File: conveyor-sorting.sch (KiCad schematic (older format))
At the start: 17 parts

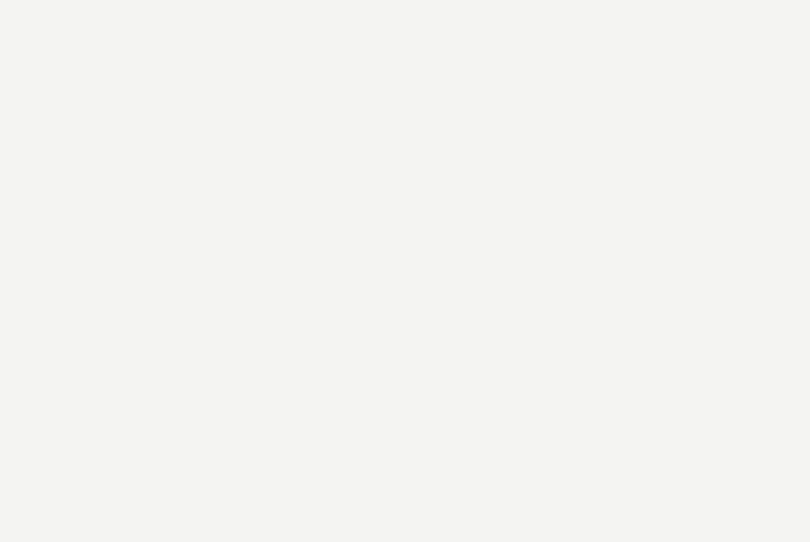
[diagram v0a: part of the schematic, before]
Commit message: Added l293d lib
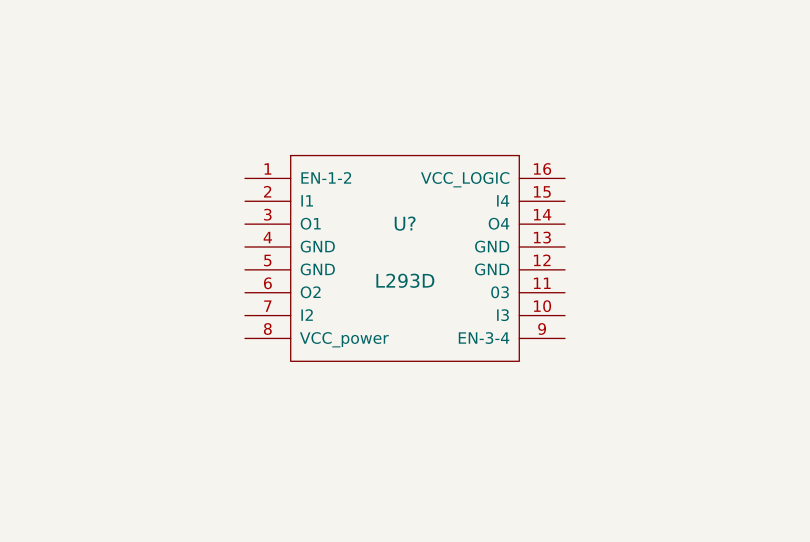
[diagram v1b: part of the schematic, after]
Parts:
- added U?: L293D, symbol L293D
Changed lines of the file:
@@
 LIBS:contrib
 LIBS:valves
+LIBS:l293d
+LIBS:conveyor-sorting-cache
 EELAYER 25 0
 EELAYER END
@@
 Text Label 6700 4400 2    60   ~ 0
 M3_Signal
+$Comp
+L L293D U?
+U 1 1 58CEFBD8
+P 7650 2200
+F 0 "U?" H 7650 2350 60  0000 C CNN
+F 1 "L293D" H 7650 2100 60  0000 C CNN
+F 2 "" H 7650 2000 60  0001 C CNN
+F 3 "" H 7650 2000 60  0001 C CNN
+	1    7650 2200
+	1    0    0    -1
+$EndComp
 $EndSCHEMATC

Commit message: rev 1 done
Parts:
- removed U?: L293D, symbol L293D
- added P1, P2: CONN_01X02, Terminal_Blocks:TerminalBlock_Pheonix_MKDS1.5-2pol, symbol CONN_01X02
- added P15: CONN_01X07, Connectors_Molex:Molex_KK-6410-07_07x2.54mm_Straight, symbol CONN_01X07
- added P16, P18, P3: CONN_01X02, Connectors_Molex:Molex_KK-6410-02_02x2.54mm_Straight, symbol CONN_01X02
- added P17, P8: CONN_01X03, Connectors_Molex:Molex_KK-6410-03_03x2.54mm_Straight, symbol CONN_01X03
- added P19: CONN_01X05, Connectors_Molex:Molex_KK-6410-05_05x2.54mm_Straight, symbol CONN_01X05
- added P20: CONN_01X05, Modified Footprints:TerminalBlock_Pheonix_MKDS1.5-5pol, symbol CONN_01X05
- added U1: L293D, Housings_DIP:DIP-16_W7.62mm_LongPads, symbol L293D
- P10, P11, P13, P9: renamed from P?; footprint (none) -> Terminal_Blocks:TerminalBlock_Pheonix_MKDS1.5-2pol
- P12, P14: renamed from P?; footprint (none) -> Terminal_Blocks:TerminalBlock_Pheonix_MKDS1.5-3pol
- P4, P5, P6, P7: renamed from P?; footprint (none) -> Connectors_Molex:Molex_KK-6410-03_03x2.54mm_Straight
- R1, R2, R3, R4: renamed from R?; footprint (none) -> Resistors_ThroughHole:R_Axial_DIN0207_L6.3mm_D2.5mm_P10.16mm_Horizontal
- U2: renamed from U?; footprint (none) -> Housings_DIP:DIP-16_W7.62mm_LongPads
- U3, U4: renamed from U?; footprint DIP-6 -> Housings_DIP:DIP-6_W7.62mm_LongPads
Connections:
- net +12V: now also P20.5 (P5), U1.8 (VCC_power)
- net GND: now also P16.1 (P1), P8.2 (P2), U1.12 (GND), U1.13 (GND), U1.4 (GND), U1.5 (GND)
- net IR_1: now also P15.5 (P5)
- net IR_2: now also P15.4 (P4)
- net IR_3: now also P15.3 (P3)
- net IR_4: now also P15.2 (P2)
- net M1_Signal: now also P18.1 (P1)
- net M2_Signal: now also P18.2 (P2)
- net PROX_1: now also P15.6 (P6)
- net PROX_2: now also P15.7 (P7)
- net VCC: now also P16.2 (P2), P8.1 (P1), U1.1 (EN-1-2), U1.16 (VCC_LOGIC)
- net at U2.10 (O7): now also P20.4 (P4)
- net at U2.11 (O6): now also P20.3 (P3)
- net at U2.12 (O5): now also P20.2 (P2)
- net at U2.13 (O4): now also P20.1 (P1)
- net at U2.4 (I4): now also P19.4 (P4)
- net at U2.5 (I5): now also P19.3 (P3)
- net at U2.6 (I6): now also P19.2 (P2)
- net at U2.7 (I7): now also P19.1 (P1)
- net M3_Signal: no longer names the net of U2.3 (I3)
- net M3_Signal: now also P19.5 (P5)
- new net: P2.1 (P1), U1.14 (O4)
- new net: P2.2 (P2), U1.11 (03)
- new net: P1.1 (P1), U1.6 (O2)
- new net: P1.2 (P2), U1.3 (O1)
- new net: P17.3 (P3), U1.9 (EN-3-4)
- new net IN1: P3.1 (P1), U1.2 (I1)
- new net IN2: P3.2 (P2), U1.7 (I2)
- new net IN3: P17.1 (P1), U1.10 (I3)
- new net IN4: P17.2 (P2), U1.15 (I4)
- new net IR_5: P15.1 (P1), P8.3 (P3)
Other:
- moved on the sheet: P12, P14, P4, P5, P6, P7, R1, R2, R3, R4, U3, U4
